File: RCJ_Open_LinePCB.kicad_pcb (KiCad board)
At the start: 4 copper layers, 180 x 171.9 mm, 205 parts, among them J1 Conn_01x12, U1 MCP3008, U2 MCP3008, U3 MCP3008, U4 MCP3008, U5 MCP3008, U6 MCP3008

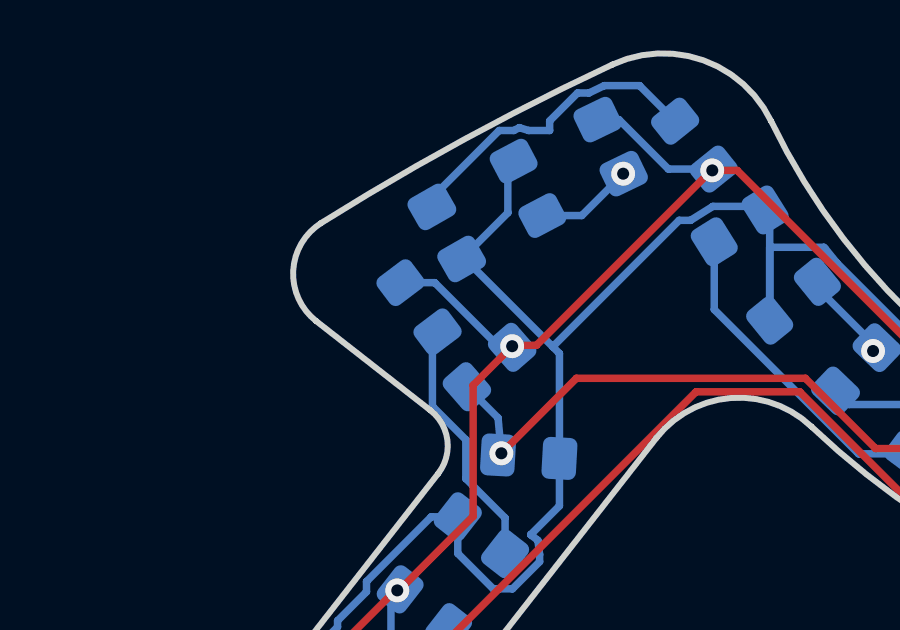
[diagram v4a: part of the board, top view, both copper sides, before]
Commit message: fixed copper sliver
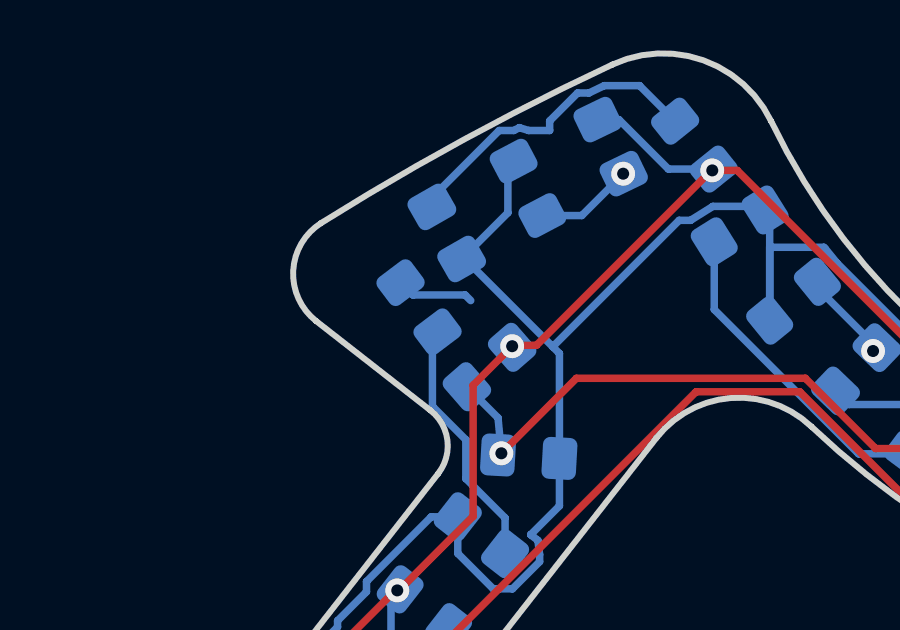
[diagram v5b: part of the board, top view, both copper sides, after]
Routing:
- net GND: track 988.3 -> 986.7 mm
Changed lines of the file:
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@@
 		)
 		(fp_line
-			(start -1.860003 0.96)
+			(start -1.860004 0.96)
 			(end -1.86 -0.96)
 			(stroke
@@
 		(fp_line
 			(start 1 0.96)
-			(end -1.860003 0.96)
+			(end -1.860004 0.96)
 			(stroke
 				(width 0.12)
@@
 	)
 	(segment
+		(start 58.0696 20.812622)
+		(end 59.812622 20.812622)
+		(width 0.25)
+		(layer "B.Cu")
+		(net 1)
+	)
+	(segment
 		(start 136.273992 15.486482)
 		(end 136.467122 15.486482)
@@
 	)
 	(segment
-		(start 60.95671 22.557817)
-		(end 58.80091 20.402017)
-		(width 0.25)
-		(layer "B.Cu")
-		(net 1)
-	)
-	(segment
 		(start 14.297528 98.085816)
 		(end 16.213304 96.17004)
@@
 	)
 	(segment
+		(start 57.658995 20.402017)
+		(end 58.0696 20.812622)
+		(width 0.25)
+		(layer "B.Cu")
+		(net 1)
+	)
+	(segment
 		(start 109.677918 182.902535)
 		(end 107.847026 181.071643)
@@
 	)
 	(segment
+		(start 59.812622 20.812622)
+		(end 60 21)
+		(width 0.25)
+		(layer "B.Cu")
+		(net 1)
+	)
+	(segment
 		(start 155.874416 44.038786)
 		(end 154.687483 42.851853)
@@
 		(width 0.25)
 		(layer "B.Cu")
-		(net 1)
-	)
-	(segment
-		(start 58.80091 20.402017)
-		(end 57.658995 20.402017)
-		(width 0.25)
-		(layer "B.Cu")
